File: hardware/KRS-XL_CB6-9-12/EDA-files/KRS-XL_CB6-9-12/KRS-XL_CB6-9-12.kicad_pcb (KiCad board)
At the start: 2 copper layers, 207.5 x 40.6 mm, 55 parts, among them J1 KNX / GND, J2 Conn_02x10_Odd_Even, J3 KNX / GND, SW1 SW_Push_Dual, SW10 SW_Push_Dual, SW11 SW_Push_Dual, SW12 SW_Push_Dual, SW13 SW_Push_Dual, SW14 SW_Push_Dual, SW15 SW_Push_Dual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

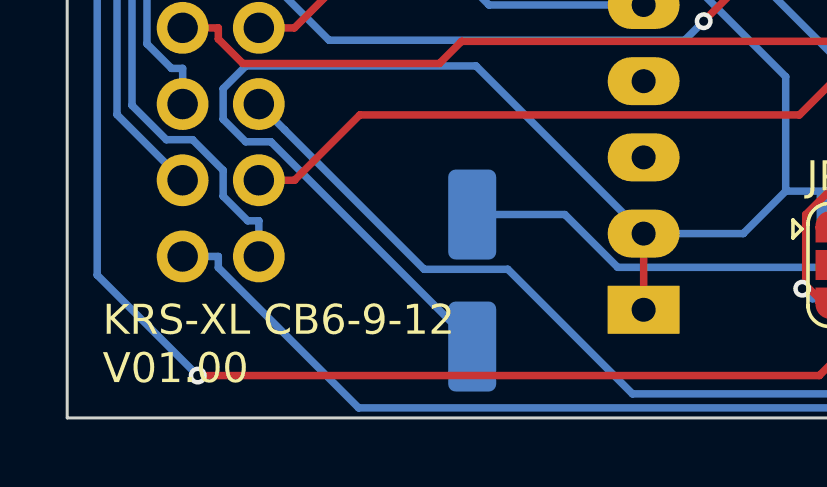
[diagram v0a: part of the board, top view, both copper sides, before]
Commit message: worked on V01.01 - RST of ItsyBitsy disconnected from 3v3
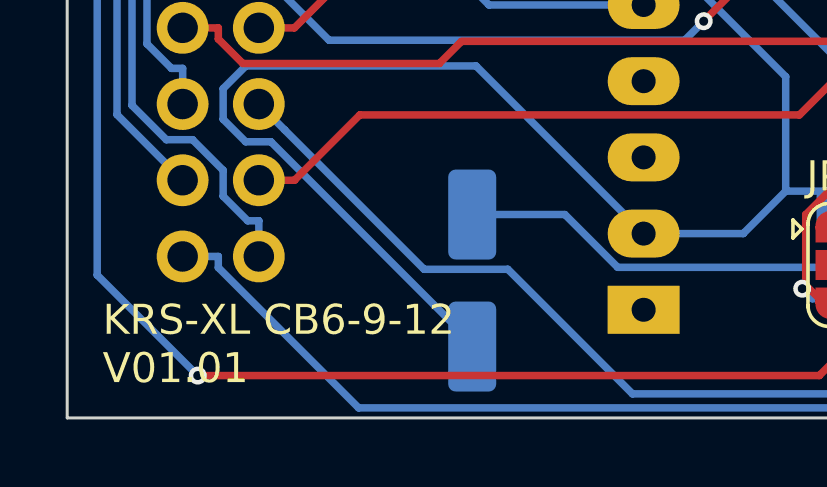
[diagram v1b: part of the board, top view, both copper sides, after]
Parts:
- C1, C2: value C -> 47nF
- R1: value R -> 680R
- R2: value R -> 850R
- R3: value R -> 550R
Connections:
- GN2 pad 1: +3V3 -> Net-(GN2-Pad1)
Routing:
- net +3V3: track 190.1 -> 187.5 mm
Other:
- board text added: "KRS-XL CB6-9-12 V01.01"
- board text removed: "KRS-XL CB6-9-12 V01.00"
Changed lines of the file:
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@@
     (thickness 1.6)
     (drawings 9)
-    (tracks 960)
+    (tracks 959)
     (zones 0)
     (modules 55)
-    (nets 61)
+    (nets 62)
   )
   (page A4)
   (title_block
     (title "KRS-XL CB6-9-12")
-    (date 2019-11-08)
-    (rev V01.00)
+    (date 2020-01-10)
+    (rev V01.01_work)
     (company "SirSydom KNX Labs")
     (comment 2 com@sirsydom.de)
@@
     (35 F.Paste user hide)
     (36 B.SilkS user)
-    (37 F.SilkS user)
+    (37 F.SilkS user hide)
     (38 B.Mask user)
-    (39 F.Mask user)
+    (39 F.Mask user hide)
     (40 Dwgs.User user)
     (41 Cmts.User user)
@@
     (45 Margin user)
     (46 B.CrtYd user)
-    (47 F.CrtYd user)
+    (47 F.CrtYd user hide)
     (48 B.Fab user hide)
     (49 F.Fab user hide)
@@
     (visible_elements 7FFFFFFF)
     (pcbplotparams
-      (layerselection 0x01030_ffffffff)
+      (layerselection 0x010f0_ffffffff)
       (usegerberextensions false)
       (usegerberattributes false)
@@
   (net 59 "Net-(GN2-Pad28)")
   (net 60 "Net-(J2-Pad10)")
+  (net 61 "Net-(GN2-Pad1)")
   (net_class Default "This is the default net class."
     (clearance 0.2)
@@
     (add_net "Net-(GN1-Pad6)")
     (add_net "Net-(GN1-Pad7)")
+    (add_net "Net-(GN2-Pad1)")
     (add_net "Net-(GN2-Pad15)")
     (add_net "Net-(GN2-Pad16)")
@@
       (effects (font (size 1 1) (thickness 0.15)) (justify mirror))
     )
-    (fp_text value C (at 0 -1.82 270) (layer B.Fab)
+    (fp_text value 47nF (at 0 -1.82 270) (layer B.Fab)
       (effects (font (size 1 1) (thickness 0.15)) (justify mirror))
     )
@@
       (effects (font (size 1 1) (thickness 0.15)))
     )
-    (fp_text value C (at 0 1.82 90) (layer F.Fab)
+    (fp_text value 47nF (at 0 1.82 90) (layer F.Fab)
       (effects (font (size 1 1) (thickness 0.15)))
     )
@@
       (effects (font (size 1 1) (thickness 0.15)))
     )
-    (fp_text value R (at 0 1.82 90) (layer F.Fab)
+    (fp_text value 680R (at 0 1.82 90) (layer F.Fab)
       (effects (font (size 1 1) (thickness 0.15)))
     )
@@
       (effects (font (size 1 1) (thickness 0.15)))
     )
-    (fp_text value R (at 0 1.82 270) (layer F.Fab)
+    (fp_text value 850R (at 0 1.82 270) (layer F.Fab)
       (effects (font (size 1 1) (thickness 0.15)))
     )
@@
       (effects (font (size 1 1) (thickness 0.15)))
     )
-    (fp_text value R (at 0 1.82 90) (layer F.Fab)
+    (fp_text value 550R (at 0 1.82 90) (layer F.Fab)
       (effects (font (size 1 1) (thickness 0.15)))
     )
@@
       (net 12 "Net-(GN2-Pad15)"))
     (pad 1 thru_hole rect (at 0 0) (size 2.4 1.6) (drill 0.8) (layers *.Cu *.Mask)
-      (net 10 +3V3))
+      (net 61 "Net-(GN2-Pad1)"))
   )
   (module Package_SO:SOIC-8_3.9x4.9mm_P1.27mm (layer F.Cu)
@@
   )
   (gr_line (start 205.5 50) (end 205.5 90.6) (layer F.SilkS) (width 0.15))
-  (gr_text "KRS-XL CB6-9-12\nV01.00" (at 51.181 88.138) (layer F.SilkS)
+  (gr_text "KRS-XL CB6-9-12\nV01.01" (at 51.181 88.138) (layer F.SilkS)
     (effects (font (size 1 1) (thickness 0.15)) (justify left))
   )
@@
   (segment (start 66.588996 83.82) (end 68.349006 85.58001) (width 0.25) (layer B.Cu) (net 9))
   (segment (start 63.5 83.82) (end 66.588996 83.82) (width 0.25) (layer B.Cu) (net 9))
+  (segment (start 193.189 57.368) (end 194.564 57.368) (width 0.25) (layer F.Cu) (net 9))
+  (segment (start 194.564 52.868) (end 193.189 52.868) (width 0.25) (layer F.Cu) (net 9))
+  (segment (start 193.78 87.975) (end 193.78 83.475) (width 0.25) (layer F.Cu) (net 9))
+  (segment (start 193.78 83.475) (end 193.78 52.995) (width 0.25) (layer F.Cu) (net 9))
+  (segment (start 192.48 67.655) (end 193.78 67.655) (width 0.25) (layer F.Cu) (net 9))
+  (segment (start 191.241999 68.893001) (end 192.48 67.655) (width 0.25) (layer F.Cu) (net 9))
+  (segment (start 178.573999 68.893001) (end 191.241999 68.893001) (width 0.25) (layer F.Cu) (net 9))
+  (segment (start 172.882297 63.201299) (end 178.573999 68.893001) (width 0.25) (layer F.Cu) (net 9))
+  (segment (start 117.093959 63.201299) (end 172.882297 63.201299) (width 0.25) (layer F.Cu) (net 9))
+  (segment (start 116.63066 62.738) (end 117.093959 63.201299) (width 0.25) (layer F.Cu) (net 9))
+  (segment (start 115.57 62.738) (end 116.63066 62.738) (width 0.25) (layer F.Cu) (net 9))
   (segment (start 75.7285 59.4725) (end 73.8973 57.6413) (width 0.25) (layer B.Cu) (net 10))
   (segment (start 73.8973 57.6413) (end 66.2196 57.6413) (width 0.25) (layer B.Cu) (net 10))
@@
   (via (at 92.1851 53.0979) (size 0.6) (layers F.Cu B.Cu) (net 10))
   (via (at 65.7459 57.1676) (size 0.6) (layers F.Cu B.Cu) (net 10))
-  (segment (start 69.215 84.455) (end 69.215 86.995) (width 0.25) (layer F.Cu) (net 10))
   (segment (start 88.9043 73.6557) (end 88.9 73.66) (width 0.25) (layer B.Cu) (net 11))
   (segment (start 91.44 73.152) (end 89.408 73.152) (width 0.25) (layer B.Cu) (net 11))
@@
   (segment (start 74.4072 80.5004) (end 78.0726 76.835) (width 0.25) (layer F.Cu) (net 34))
   (segment (start 78.0726 76.835) (end 84.455 76.835) (width 0.25) (layer F.Cu) (net 34))
-  (segment (start 193.189 57.368) (end 194.564 57.368) (width 0.25) (layer F.Cu) (net 9))
-  (segment (start 194.564 52.868) (end 193.189 52.868) (width 0.25) (layer F.Cu) (net 9))
-  (segment (start 193.78 87.975) (end 193.78 83.475) (width 0.25) (layer F.Cu) (net 9))
-  (segment (start 193.78 83.475) (end 193.78 52.995) (width 0.25) (layer F.Cu) (net 9))
-  (segment (start 192.48 67.655) (end 193.78 67.655) (width 0.25) (layer F.Cu) (net 9))
-  (segment (start 191.241999 68.893001) (end 192.48 67.655) (width 0.25) (layer F.Cu) (net 9))
-  (segment (start 178.573999 68.893001) (end 191.241999 68.893001) (width 0.25) (layer F.Cu) (net 9))
-  (segment (start 172.882297 63.201299) (end 178.573999 68.893001) (width 0.25) (layer F.Cu) (net 9))
-  (segment (start 117.093959 63.201299) (end 172.882297 63.201299) (width 0.25) (layer F.Cu) (net 9))
-  (segment (start 116.63066 62.738) (end 117.093959 63.201299) (width 0.25) (layer F.Cu) (net 9))
-  (segment (start 115.57 62.738) (end 116.63066 62.738) (width 0.25) (layer F.Cu) (net 9))
   (segment (start 131.5 61.17) (end 131.5 60.4823) (width 0.25) (layer F.Cu) (net 34))
   (segment (start 143.549 89.1878) (end 144.496 89.1878) (width 0.25) (layer F.Cu) (net 34))
